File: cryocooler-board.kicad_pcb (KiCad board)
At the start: 4 copper layers, 58 x 49 mm, 50 parts, among them J1 MOL Pico 4, J2 MOL Pico 4, J3 MOL Pico 4, J4 MOL Pico 4, Q1 IPZ40N04S5-3R1, Q2 IPZ40N04S5-3R1, U1 PTPS55288RPMR, U2 AD5258BRMZ1, U3 C1T 4

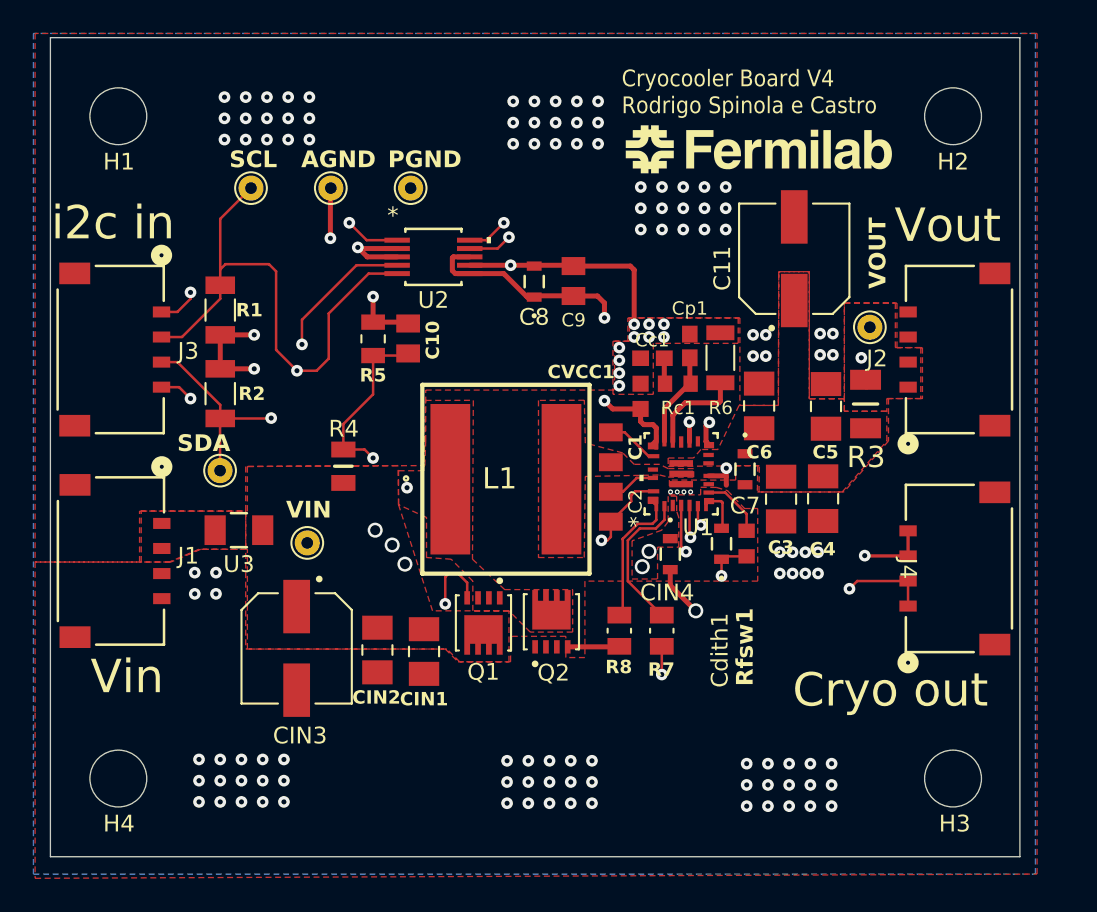
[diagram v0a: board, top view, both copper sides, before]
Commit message: Reorganize libraries: lib/Cryocooler symbols, footprints and 3D models; custom NT1 net tie; L1 symbol corrected to XAL1010-103MED; add 2-pin Molex for future use
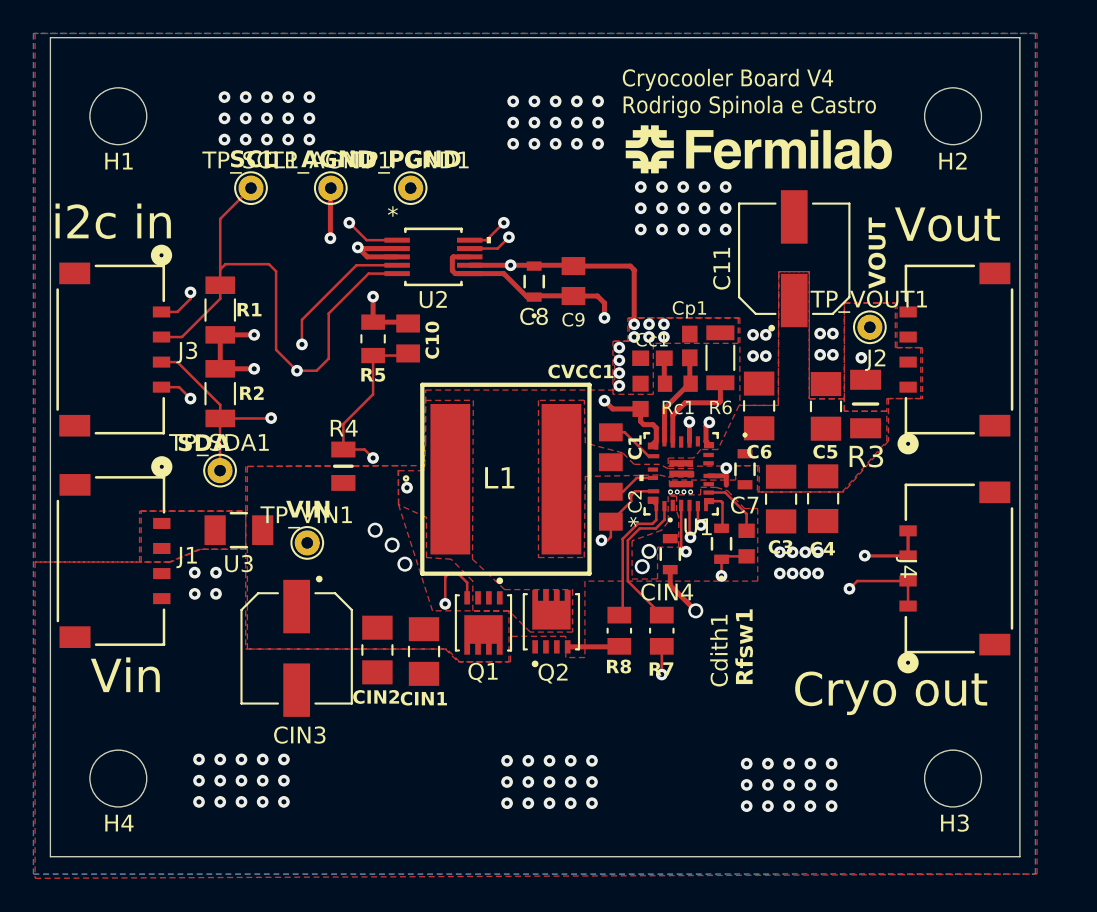
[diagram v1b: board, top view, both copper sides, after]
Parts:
- C1, C10, C2, C9: footprint Cryocooler_footprints:GCM21BR72A104KA37L -> Cryocooler:GCM21BR72A104KA37L
- C11, CIN3: footprint Cryocooler_footprints:EEH-ZA1V680XP -> Cryocooler:EEH-ZA1V680XP
- C3, C4, C5, C6, CIN1, CIN2: footprint Cryocooler_footprints:CGA5L1X7R1H106K160AC -> Cryocooler:CGA5L1X7R1H106K160AC
- C7, C8, CIN4: footprint Cryocooler_footprints:CGA3E3X5R1H105M080AB -> Cryocooler:CGA3E3X5R1H105M080AB
- CVCC1: footprint Cryocooler_footprints:GRT188R61C475KE13D -> Cryocooler:GRT188R61C475KE13D
- Cc1: footprint Cryocooler_footprints:CGA3E2C0G1H562J080AA -> Cryocooler:CGA3E2C0G1H562J080AA
- Cdith1: footprint Cryocooler_footprints:CGA3E2X7R1H473K080AD -> Cryocooler:CGA3E2X7R1H473K080AD
- Cp1: footprint Cryocooler_footprints:CGA3E2NP01H220J080AA -> Cryocooler:CGA3E2NP01H220J080AA
- H1, H2, H3, H4: footprint Cryocooler_footprints:M3_3_4mm_hole -> Cryocooler:M3_3_4mm_hole
- J1, J2, J3, J4: footprint Cryocooler_footprints:MOLEX_4_pin -> Cryocooler:MOLEX_4_pin
- L1: footprint Cryocooler_footprints:XAL1010 -> Cryocooler:XAL1010
- NT1: footprint NetTie:NetTie-2_SMD_Pad0.5mm -> Cryocooler:NetTie-2_SMD_Pad0.3mm
- Q1, Q2: footprint Cryocooler_footprints:IPZ40N04S5L4R8ATMA1 -> Cryocooler:IPZ40N04S5L4R8ATMA1
- R1, R2: footprint Cryocooler_footprints:CRCW12062K20JNEA -> Cryocooler:CRCW12062K20JNEA
- R3: footprint Cryocooler_footprints:CRF1206-FZ-R010ELF -> Cryocooler:CRF1206-FZ-R010ELF
- R4: footprint Cryocooler_footprints:CRCW080530K9FKEA -> Cryocooler:CRCW080530K9FKEA
- R5: footprint Cryocooler_footprints:CRCW08052K00FKEA -> Cryocooler:CRCW08052K00FKEA
- R6: footprint Cryocooler_footprints:CRCW120620K0FKEAC -> Cryocooler:CRCW120620K0FKEAC
- R7, R8: footprint Cryocooler_footprints:CRCW08051R00JNEAHP -> Cryocooler:CRCW08051R00JNEAHP
- Rc1: footprint Cryocooler_footprints:CRCW060326K1FKEA -> Cryocooler:CRCW060326K1FKEA
- Rfsw1: footprint Cryocooler_footprints:CRCW060310K0FKEA -> Cryocooler:CRCW060310K0FKEA
- U1: footprint Cryocooler_footprints:TPS55288 -> Cryocooler:TPS55288
- U2: footprint Cryocooler_footprints:AD5258BRMZ1_IC -> Cryocooler:AD5258BRMZ1_IC
- U3: footprint Cryocooler_footprints:0685T4000-01 -> Cryocooler:0685T4000-01

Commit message: V4.1:Cryocooler VOUT connector changed to 2-pin Pico-Lock 2053380002 (J5); R3 and TP_VOUT1 moved
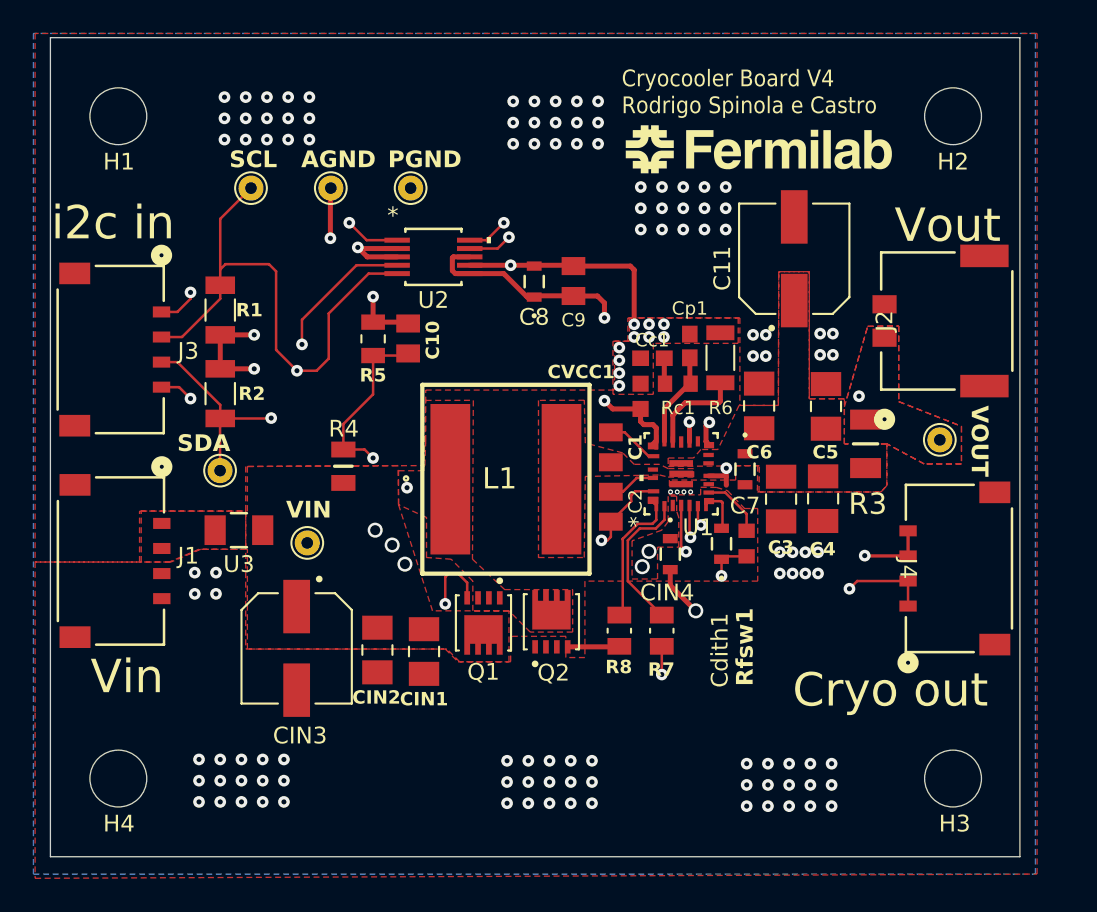
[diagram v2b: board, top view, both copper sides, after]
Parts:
- Cdith1: value 0.047uF -> 15nF
- J2: value MOL Pico 4 -> MOL Pico 2; footprint Cryocooler:MOLEX_4_pin -> Cryocooler:MOLEX_2_pin
- moved TP_VOUT1 7.93 mm to (161.2, 85.2)
- moved R3 2.38 mm to (156.7, 85.5)
- moved J2 1.86 mm to (161.6, 78.1), turned to 90 degrees
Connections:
- J2 pad 2: VOUT -> PGND
- J2 pad 3: PGND -> (no net)
- J2 pad 4: PGND -> (no net)
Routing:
- net VOUT: track 12.4 -> 11.2 mm

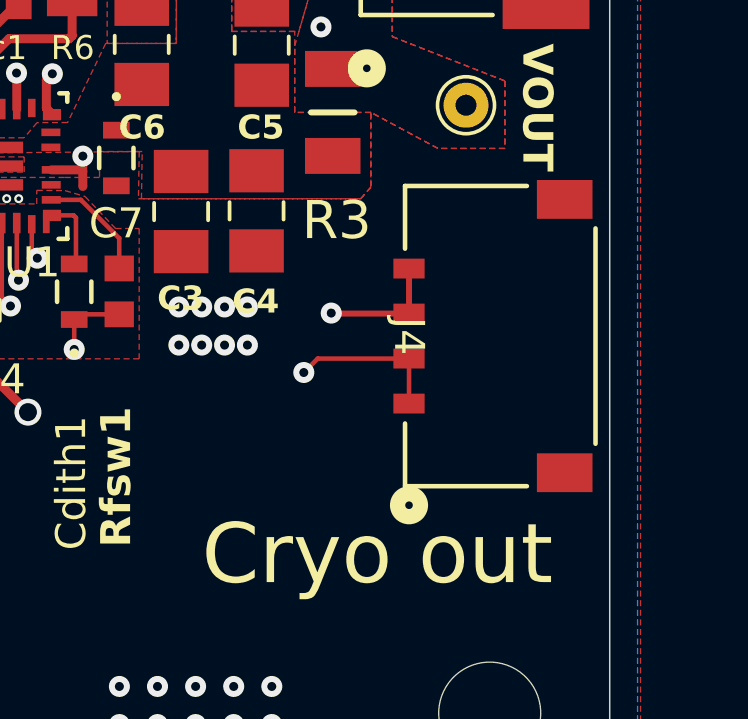
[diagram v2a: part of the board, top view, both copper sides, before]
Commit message: V4.1: J4 (cryocooler set point) back to 2-pin Pico-Lock 2053380002; CRYO_1/CRYO_2 rerouted
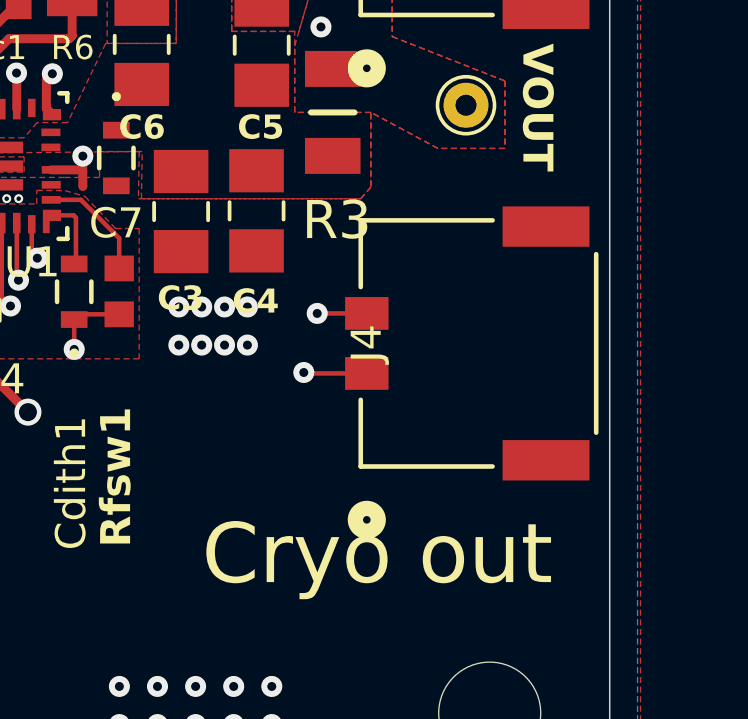
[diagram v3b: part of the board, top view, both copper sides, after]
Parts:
- J4: footprint Cryocooler:MOLEX_4_pin -> Cryocooler:MOLEX_2_pin
- moved J4 0.77 mm to (161.6, 93.2), turned to 90 degrees
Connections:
- J4 pad 2: CRYO_2 -> CRYO_1
- J4 pad 3: CRYO_1 -> (no net)
- J4 pad 4: CRYO_1 -> (no net)
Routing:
- net CRYO_2: track 51.0 -> 48.6 mm
- net CRYO_1: track 61.5 -> 59.3 mm
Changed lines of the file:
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@@
 		)
 	)
-	(footprint "Cryocooler:MOLEX_4_pin"
+	(footprint "Cryocooler:MOLEX_2_pin"
 		(layer "F.Cu")
-		(at 162.327001 92.93 -90)
-		(tags "5040500491 ")
+		(at 161.6 93.175 90)
+		(tags "2053380002 ")
 		(property "Reference" "J4"
-			(at 0 3.042001 -90)
+			(at 0 -3.722299 90)
 			(unlocked yes)
 			(layer "F.SilkS")
@@
 		)
 		(property "Value" "MOL Pico 4"
-			(at 0 3.042001 -90)
+			(at 0 -3.722299 90)
 			(unlocked yes)
 			(layer "F.Fab")
@@
 			)
 		)
-		(property "Footprint" "Cryocooler:MOLEX_4_pin"
+		(property "Footprint" "Cryocooler:MOLEX_2_pin"
 			(at 0 0 90)
 			(layer "F.Fab")
@@
 			)
 		)
-		(property "Datasheet" "https://www.molex.com/en-us/products/part-detail-pdf/5040500491?display=pdf"
+		(property "Datasheet" "https://www.molex.com/en-us/products/part-detail-pdf/2053380002?display=pdf"
 			(at 0 0 90)
 			(layer "F.Fab")
@@
 			)
 		)
-		(property ki_fp_filters "CONN_5040500491_MOL")
+		(property ki_fp_filters "CONN_2053380000-SD_02_MOL")
 		(sheetname "Root")
 		(sheetfile "cryocooler-board.kicad_sch")
 		(attr smd)
 		(fp_circle
-			(center 5.6388 3.042001)
-			(end 6.0198 3.042001)
+			(center -5.8801 -3.722299)
+			(end -5.4991 -3.722299)
 			(stroke
 				(width 0.508)
@@
 		)
 		(fp_line
-			(start -5.0038 3.175)
-			(end -2.912941 3.175)
+			(start 4.1021 -3.924299)
+			(end 1.878841 -3.924299)
 			(stroke
 				(width 0.1524)
@@
 		)
 		(fp_line
-			(start 2.912941 3.175)
-			(end 5.0038 3.175)
+			(start -1.878841 -3.924299)
+			(end -4.1021 -3.924299)
 			(stroke
 				(width 0.1524)
@@
 		)
 		(fp_line
-			(start 5.0038 3.175)
-			(end 5.0038 -0.888159)
+			(start -4.1021 -3.924299)
+			(end -4.1021 0.472161)
 			(stroke
 				(width 0.1524)
@@
 		)
 		(fp_line
-			(start -5.0038 -0.888159)
-			(end -5.0038 3.175)
+			(start 4.1021 0.472161)
+			(end 4.1021 -3.924299)
 			(stroke
 				(width 0.1524)
@@
 		)
 		(fp_line
-			(start 3.589911 -3.175)
-			(end -3.589911 -3.175)
+			(start -2.97567 3.9243)
+			(end 2.97567 3.9243)
 			(stroke
 				(width 0.1524)
@@
 		)
 		(fp_circle
-			(center 5.6388 3.042001)
-			(end 6.0198 3.042001)
+			(center -5.8801 -3.722299)
+			(end -5.4991 -3.722299)
 			(stroke
 				(width 0.508)
@@
 		)
 		(fp_line
-			(start -5.4567 3.816701)
-			(end 5.4567 3.816701)
+			(start 4.822101 -4.700199)
+			(end -4.822101 -4.700199)
 			(stroke
 				(width 0.1524)
@@
 		)
 		(fp_line
-			(start 5.4567 3.816701)
-			(end 5.4567 -3.329099)
+			(start -4.822101 -4.700199)
+			(end -4.822101 4.0513)
 			(stroke
 				(width 0.1524)
@@
 		)
 		(fp_line
-			(start -5.4567 -3.329099)
-			(end -5.4567 3.816701)
+			(start 4.822101 4.0513)
+			(end 4.822101 -4.700199)
 			(stroke
 				(width 0.1524)
@@
 		)
 		(fp_line
-			(start 5.4567 -3.329099)
-			(end -5.4567 -3.329099)
+			(start -4.822101 4.0513)
+			(end 4.822101 4.0513)
 			(stroke
 				(width 0.1524)
@@
 		)
 		(fp_line
-			(start -4.8768 3.048)
-			(end 4.8768 3.048)
+			(start 3.9751 -3.797299)
+			(end -3.9751 -3.797299)
 			(stroke
 				(width 0.0254)
@@
 		)
 		(fp_line
-			(start 4.8768 3.048)
-			(end 4.8768 -3.048)
+			(start -3.9751 -3.797299)
+			(end -3.9751 3.7973)
 			(stroke
 				(width 0.0254)
@@
 		)
 		(fp_line
-			(start -4.8768 -3.048)
-			(end -4.8768 3.048)
+			(start 3.9751 3.7973)
+			(end 3.9751 -3.797299)
 			(stroke
 				(width 0.0254)
@@
 		)
 		(fp_line
-			(start 4.8768 -3.048)
-			(end -4.8768 -3.048)
+			(start -3.9751 3.7973)
+			(end 3.9751 3.7973)
 			(stroke
 				(width 0.0254)
@@
 		)
 		(fp_circle
-			(center 2.25 4.947001)
-			(end 2.631 4.947001)
+			(center -1 -5.627299)
+			(end -0.619 -5.627299)
 			(stroke
 				(width 0.508)
@@
 		)
 		(fp_text user "${REFERENCE}"
-			(at 0 3.042001 -90)
+			(at 0 -3.722299 90)
 			(unlocked yes)
 			(layer "F.Fab")
@@
 		)
 		(pad "1" smd rect
-			(at 2.250001 3.042001 270)
-			(size 0.6604 1.0414)
+			(at -1.000001 -3.722299 90)
+			(size 1.0922 1.4478)
 			(layers "F.Cu" "F.Paste" "F.Mask")
 			(net 5 "CRYO_2")
@@
 		)
 		(pad "2" smd rect
-			(at 0.750001 3.042001 270)
-			(size 0.6604 1.0414)
+			(at 1.000001 -3.722299 90)
+			(size 1.0922 1.4478)
 			(layers "F.Cu" "F.Paste" "F.Mask")
-			(net 5 "CRYO_2")
+			(net 6 "CRYO_1")
 			(pinfunction "2")
 			(pintype "unspecified")
 		)
 		(pad "3" smd rect
-			(at -0.750001 3.042001 270)
-			(size 0.6604 1.0414)
+			(at -3.895001 2.252701 90)
+			(size 1.3462 2.8956)
 			(layers "F.Cu" "F.Paste" "F.Mask")
-			(net 6 "CRYO_1")
-			(pinfunction "3")
-			(pintype "unspecified")
 		)
 		(pad "4" smd rect
-			(at -2.250001 3.042001 270)
-			(size 0.6604 1.0414)
-			(layers "F.Cu" "F.Paste" "F.Mask")
-			(net 6 "CRYO_1")
-			(pinfunction "4")
-			(pintype "unspecified")
-		)
-		(pad "5" smd rect
-			(at -4.555 -2.147999 270)
-			(size 1.2954 1.8542)
-			(layers "F.Cu" "F.Paste" "F.Mask")
-		)
-		(pad "6" smd rect
-			(at 4.555 -2.147999 270)
-			(size 1.2954 1.8542)
+			(at 3.895001 2.252701 90)
+			(size 1.3462 2.8956)
 			(layers "F.Cu" "F.Paste" "F.Mask")
 		)
-		(model "${KIPRJMOD}/lib/Cryocooler.3dshapes/MOLEX_4_pin.stp"
+		(model "${KIPRJMOD}/lib/Cryocooler.3dshapes/MOLEX_2_pin.stp"
 			(offset
-				(xyz -2.25 5.25 0)
+				(xyz 1 -7.5 0)
 			)
 			(scale
@@
 			)
 			(rotate
-				(xyz 0 0 -180)
+				(xyz 0 0 0)
 			)
 		)
@@
 	)
 	(segment
-		(start 156.241999 93.680001)
-		(end 159.285 93.680001)
+		(start 155.7778 94.1442)
+		(end 155.808601 94.175001)
 		(width 0.1524)
 		(layer "F.Cu")
@@
 	)
 	(segment
-		(start 134.730799 73.789201)
-		(end 133.0609 73.789201)
-		(width 0.1524)
-		(layer "F.Cu")
-		(net 5)
-	)
-	(segment
-		(start 155.7778 94.1442)
-		(end 156.241999 93.680001)
+		(start 155.808601 94.175001)
+		(end 157.877701 94.175001)
 		(width 0.1524)
 		(layer "F.Cu")
@@
 	)
 	(segment
-		(start 159.285 93.680001)
-		(end 159.285 95.180001)
+		(start 134.730799 73.789201)
+		(end 133.0609 73.789201)
 		(width 0.1524)
 		(layer "F.Cu")
@@
 	)
 	(segment
-		(start 155.7778 91.7312)
-		(end 155.7778 94.1442)
+		(start 154.975 92.534)
+		(end 154.975 93.3414)
 		(width 0.1524)
 		(layer "In2.Cu")
@@
 	)
 	(segment
-		(start 157.378 75.907)
-		(end 158.775 77.304)
+		(start 158.775 77.304)
+		(end 158.775 88.734)
 		(width 0.1524)
 		(layer "In2.Cu")
@@
 	)
 	(segment
-		(start 158.775 88.734)
-		(end 155.7778 91.7312)
+		(start 154.975 93.3414)
+		(end 155.7778 94.1442)
 		(width 0.1524)
 		(layer "In2.Cu")
@@
 	)
 	(segment
-		(start 158.775 77.304)
-		(end 158.775 88.734)
+		(start 157.378 75.907)
+		(end 158.775 77.304)
 		(width 0.1524)
 		(layer "In2.Cu")
@@
 	)
 	(segment
-		(start 135.407 73.113)
-		(end 141.503 73.113)
+		(start 141.503 73.113)
+		(end 144.297 75.907)
 		(width 0.1524)
 		(layer "In2.Cu")
@@
 	)
 	(segment
-		(start 141.503 73.113)
-		(end 144.297 75.907)
+		(start 158.775 88.734)
+		(end 154.975 92.534)
+		(width 0.1524)
+		(layer "In2.Cu")
+		(net 5)
+	)
+	(segment
+		(start 135.407 73.113)
+		(end 141.503 73.113)
 		(width 0.1524)
 		(layer "In2.Cu")
@@
 	)
 	(segment
-		(start 156.709199 92.179999)
-		(end 156.6922 92.163)
-		(width 0.2)
+		(start 156.225 92.175)
+		(end 156.475 92.175)
+		(width 0.1524)
 		(layer "F.Cu")
 		(net 6)
 	)
 	(segment
-		(start 159.285 92.179999)
-		(end 159.285 90.679999)
-		(width 0.2)
+		(start 156.475001 92.174999)
+		(end 157.877701 92.174999)
+		(width 0.1524)
 		(layer "F.Cu")
 		(net 6)
@@
 	)
 	(segment
-		(start 159.285 92.179999)
-		(end 156.709199 92.179999)
-		(width 0.2)
-		(layer "F.Cu")
-		(net 6)
-	)
-	(segment
 		(start 126.896399 73.289199)
 		(end 128.7175 73.289199)
@@
 		(net 6)
 	)
+	(segment
+		(start 156.225 92.175)
+		(end 156.225001 92.174999)
+		(width 0.1524)
+		(layer "F.Cu")
+		(net 6)
+	)
+	(segment
+		(start 156.475 92.175)
+		(end 156.475001 92.174999)
+		(width 0.1524)
+		(layer "F.Cu")
+		(net 6)
+	)
 	(via
 		(at 125.8566 72.2494)
@@
 	)
 	(via
-		(at 156.6922 92.163)
+		(at 156.225 92.175)
 		(size 0.7)
 		(drill 0.3)
@@
 	)
 	(segment
-		(start 144.5256 75.3482)
-		(end 141.4268 72.2494)
+		(start 156.225 92.175)
+		(end 159.283 89.117)
 		(width 0.1524)
 		(layer "In2.Cu")
@@
 	)
 	(segment
-		(start 156.6922 92.163)
-		(end 159.283 89.5722)
+		(start 159.283 89.117)
+		(end 159.283 76.923)
 		(width 0.1524)
 		(layer "In2.Cu")
@@
 	)
 	(segment
-		(start 159.283 89.5722)
-		(end 159.283 76.923)
+		(start 141.4268 72.2494)
+		(end 135.1022 72.2494)
 		(width 0.1524)
 		(layer "In2.Cu")
@@
 	)
 	(segment
-		(start 141.4268 72.2494)
-		(end 135.1022 72.2494)
+		(start 144.5256 75.3482)
+		(end 141.4268 72.2494)
 		(width 0.1524)
 		(layer "In2.Cu")

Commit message: V4.1: R1/R2 (I2C pull-ups) DNP for 3.3 V host; exclude DNP parts from JLC output; J4 value fixed
README: I2C level issue added to open items (provisional decision)
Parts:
- J4: value MOL Pico 4 -> MOL Pico 2
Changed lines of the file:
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@@
 		(sheetname "Root")
 		(sheetfile "cryocooler-board.kicad_sch")
-		(attr smd)
+		(attr smd dnp)
 		(fp_line
 			(start -0.64 0.88)
@@
 		(sheetname "Root")
 		(sheetfile "cryocooler-board.kicad_sch")
-		(attr smd)
+		(attr smd dnp)
 		(fp_line
 			(start -0.64 -0.88)
@@
 			)
 		)
-		(property "Value" "MOL Pico 4"
+		(property "Value" "MOL Pico 2"
 			(at 0 -3.722299 90)
 			(unlocked yes)
